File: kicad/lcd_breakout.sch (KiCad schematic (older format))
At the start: 3 parts

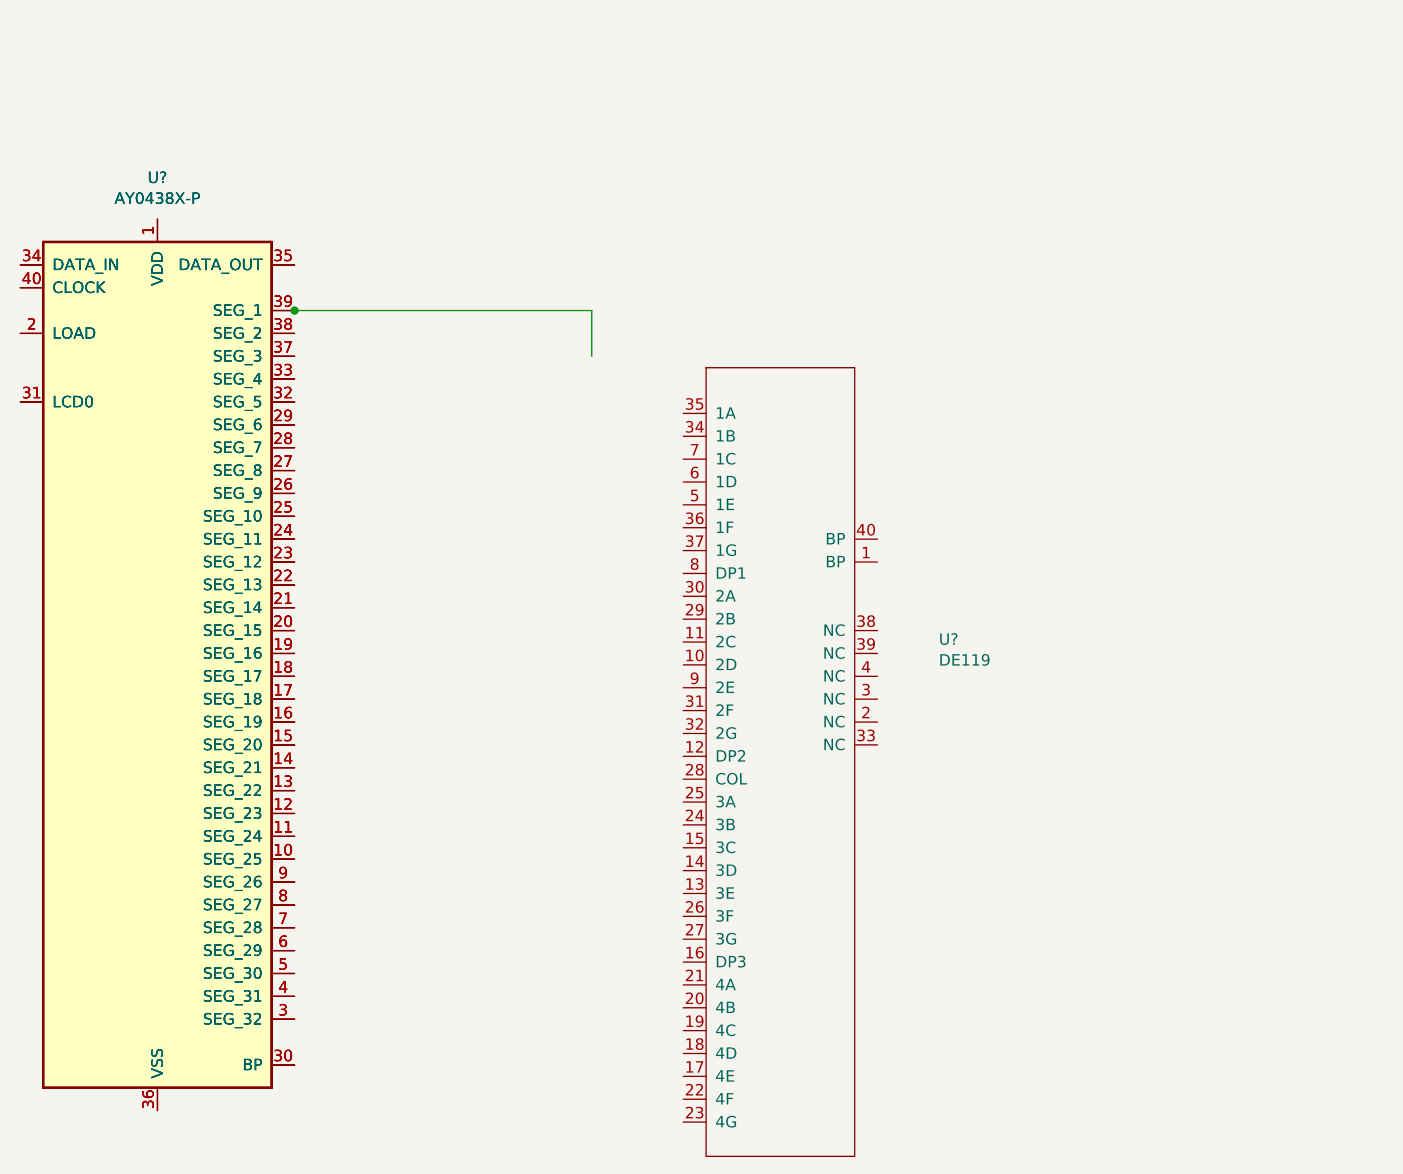
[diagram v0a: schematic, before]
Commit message: Update lcd component and schematic
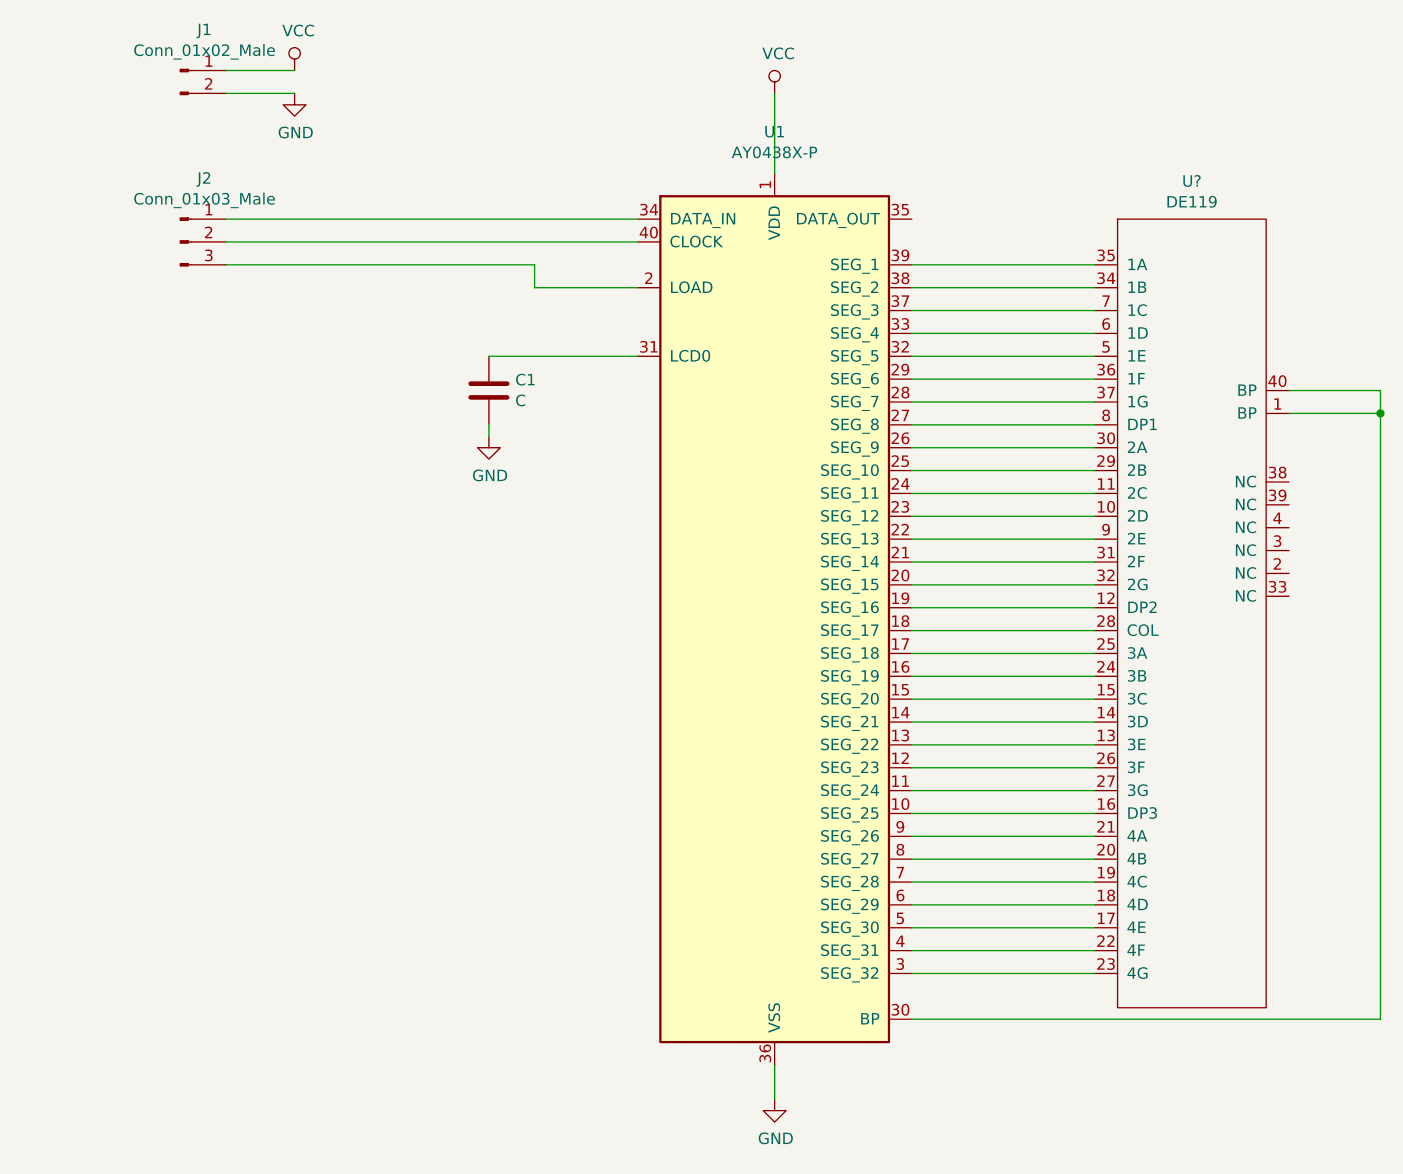
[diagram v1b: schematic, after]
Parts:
- removed U?: DE119, symbol lcd_breakout:DE119
- removed U?: AY0438X-P, Package_DIP:DIP-40_W15.24mm, symbol Driver_Display:AY0438X-P
- added C1: C, symbol Device:C
- added J1: Conn_01x02_Male, symbol Connector:Conn_01x02_Male
- added J2: Conn_01x03_Male, symbol Connector:Conn_01x03_Male
- added U?: DE119, symbol lcd_breakout:DE119
- gave numbers to parts that had none: 1
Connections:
- net labels added: GND, VCC
- wire segments 2 -> 48
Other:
- moved on the sheet: U1
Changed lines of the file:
@@
 EESchema Schematic File Version 4
-EELAYER 29 0
+LIBS:lcd_breakout-cache
+EELAYER 26 0
 EELAYER END
 $Descr A4 11693 8268
@@
 $EndDescr
 $Comp
+L Driver_Display:AY0438X-P U1
+U 1 1 5EA9573D
+P 4450 3550
+F 0 "U1" H 4450 5631 50  0000 C CNN
+F 1 "AY0438X-P" H 4450 5540 50  0000 C CNN
+F 2 "Package_DIP:DIP-40_W15.24mm" H 4450 1450 50  0001 C CNN
+F 3 "http://www.farnell.com/datasheets/43336.pdf" H 2850 4800 50  0001 C CNN
+	1    4450 3550
+	1    0    0    -1
+$EndComp
+$Comp
+L power:VCC #PWR0101
+U 1 1 5EA9E564
+P 4450 1300
+F 0 "#PWR0101" H 4450 1150 50  0001 C CNN
+F 1 "VCC" H 4467 1473 50  0000 C CNN
+F 2 "" H 4450 1300 50  0001 C CNN
+F 3 "" H 4450 1300 50  0001 C CNN
+	1    4450 1300
+	1    0    0    -1
+$EndComp
+$Comp
+L power:GND #PWR0102
+U 1 1 5EA9E718
+P 4450 5700
+F 0 "#PWR0102" H 4450 5450 50  0001 C CNN
+F 1 "GND" H 4455 5527 50  0000 C CNN
+F 2 "" H 4450 5700 50  0001 C CNN
+F 3 "" H 4450 5700 50  0001 C CNN
+	1    4450 5700
+	1    0    0    -1
+$EndComp
+Wire Wire Line
+	4450 5550 4450 5700
+Wire Wire Line
+	4450 1300 4450 1650
+$Comp
+L Connector:Conn_01x03_Male J2
+U 1 1 5EA9FA35
+P 1850 1950
+F 0 "J2" H 1956 2228 50  0000 C CNN
+F 1 "Conn_01x03_Male" H 1956 2137 50  0000 C CNN
+F 2 "" H 1850 1950 50  0001 C CNN
+F 3 "~" H 1850 1950 50  0001 C CNN
+	1    1850 1950
+	1    0    0    -1
+$EndComp
+$Comp
+L Connector:Conn_01x02_Male J1
+U 1 1 5EAA0729
+P 1850 1200
+F 0 "J1" H 1956 1378 50  0000 C CNN
+F 1 "Conn_01x02_Male" H 1956 1287 50  0000 C CNN
+F 2 "" H 1850 1200 50  0001 C CNN
+F 3 "~" H 1850 1200 50  0001 C CNN
+	1    1850 1200
+	1    0    0    -1
+$EndComp
+$Comp
+L power:GND #PWR0103
+U 1 1 5EAA09A4
+P 2350 1300
+F 0 "#PWR0103" H 2350 1050 50  0001 C CNN
+F 1 "GND" H 2355 1127 50  0000 C CNN
+F 2 "" H 2350 1300 50  0001 C CNN
+F 3 "" H 2350 1300 50  0001 C CNN
+	1    2350 1300
+	1    0    0    -1
+$EndComp
+$Comp
+L power:VCC #PWR0104
+U 1 1 5EAA0A11
+P 2350 1200
+F 0 "#PWR0104" H 2350 1050 50  0001 C CNN
+F 1 "VCC" H 2367 1373 50  0000 C CNN
+F 2 "" H 2350 1200 50  0001 C CNN
+F 3 "" H 2350 1200 50  0001 C CNN
+	1    2350 1200
+	1    0    0    -1
+$EndComp
+Wire Wire Line
+	2050 1200 2350 1200
+Wire Wire Line
+	2050 1300 2350 1300
+Wire Wire Line
+	2050 1850 3850 1850
+Wire Wire Line
+	2050 1950 3850 1950
+Wire Wire Line
+	2050 2050 3400 2050
+Wire Wire Line
+	3400 2050 3400 2150
+Wire Wire Line
+	3400 2150 3850 2150
+$Comp
+L Device:C C1
+U 1 1 5EAA22A5
+P 3200 2600
+F 0 "C1" H 3315 2646 50  0000 L CNN
+F 1 "C" H 3315 2555 50  0000 L CNN
+F 2 "" H 3238 2450 50  0001 C CNN
+F 3 "~" H 3200 2600 50  0001 C CNN
+	1    3200 2600
+	1    0    0    -1
+$EndComp
+Wire Wire Line
+	3200 2450 3850 2450
+$Comp
+L power:GND #PWR0105
+U 1 1 5EAA297E
+P 3200 2800
+F 0 "#PWR0105" H 3200 2550 50  0001 C CNN
+F 1 "GND" H 3205 2627 50  0000 C CNN
+F 2 "" H 3200 2800 50  0001 C CNN
+F 3 "" H 3200 2800 50  0001 C CNN
+	1    3200 2800
+	1    0    0    -1
+$EndComp
+Wire Wire Line
+	3200 2750 3200 2800
+$Comp
 L lcd_breakout:DE119 U?
-U 1 1 5EA94CD7
-P 4350 3900
-F 0 "U?" H 5168 4111 50  0000 L CNN
-F 1 "DE119" H 5168 4020 50  0000 L CNN
-F 2 "" H 4300 4300 50  0001 C CNN
-F 3 "" H 4300 4300 50  0001 C CNN
-	1    4350 3900
-	1    0    0    -1
-$EndComp
-$Comp
-L Driver_Display:AY0438X-P U?
-U 1 1 5EA9962D
-P 1750 3750
-F 0 "U?" H 1750 5831 50  0000 C CNN
-F 1 "AY0438X-P" H 1750 5740 50  0000 C CNN
-F 2 "Package_DIP:DIP-40_W15.24mm" H 1750 1650 50  0001 C CNN
-F 3 "http://www.farnell.com/datasheets/43336.pdf" H 150 5000 50  0001 C CNN
-	1    1750 3750
-	1    0    0    -1
-$EndComp
-$Comp
-L Driver_Display:AY0438X-P U?
-U 1 1 5EA9573D
-P 1750 3750
-F 0 "U?" H 1750 5831 50  0000 C CNN
-F 1 "AY0438X-P" H 1750 5740 50  0000 C CNN
-F 2 "Package_DIP:DIP-40_W15.24mm" H 1750 1650 50  0001 C CNN
-F 3 "http://www.farnell.com/datasheets/43336.pdf" H 150 5000 50  0001 C CNN
-	1    1750 3750
-	1    0    0    -1
-$EndComp
-Connection ~ 2350 2250
-Wire Wire Line
-	2350 2250 3650 2250
-Wire Wire Line
-	3650 2250 3650 2450
+U 1 1 5EAA427C
+P 6150 3250
+F 0 "U?" H 6275 4815 50  0000 C CNN
+F 1 "DE119" H 6275 4724 50  0000 C CNN
+F 2 "" H 7100 2450 50  0001 C CNN
+F 3 "" H 7100 2450 50  0001 C CNN
+	1    6150 3250
+	1    0    0    -1
+$EndComp
+Wire Wire Line
+	5050 2050 5850 2050
+Wire Wire Line
+	5050 2150 5850 2150
+Wire Wire Line
+	5050 2250 5850 2250
+Wire Wire Line
+	5050 2350 5850 2350
+Wire Wire Line
+	5050 2450 5850 2450
+Wire Wire Line
+	5050 2550 5850 2550
+Wire Wire Line
+	5050 2650 5850 2650
+Wire Wire Line
+	5050 2750 5850 2750
+Wire Wire Line
+	5050 2850 5850 2850
+Wire Wire Line
+	5050 2950 5850 2950
+Wire Wire Line
+	5050 3050 5850 3050
+Wire Wire Line
+	5050 3150 5850 3150
+Wire Wire Line
+	5050 3250 5850 3250
+Wire Wire Line
+	5050 3350 5850 3350
+Wire Wire Line
+	5050 3450 5850 3450
+Wire Wire Line
+	5050 3550 5850 3550
+Wire Wire Line
+	5050 3650 5850 3650
+Wire Wire Line
+	5050 3750 5850 3750
+Wire Wire Line
+	5050 3850 5850 3850
+Wire Wire Line
+	5050 3950 5850 3950
+Wire Wire Line
+	5050 4050 5850 4050
+Wire Wire Line
+	5050 4150 5850 4150
+Wire Wire Line
+	5050 4250 5850 4250
+Wire Wire Line
+	5050 4350 5850 4350
+Wire Wire Line
+	5050 4450 5850 4450
+Wire Wire Line
+	5050 4550 5850 4550
+Wire Wire Line
+	5050 4650 5850 4650
+Wire Wire Line
+	5050 4750 5850 4750
+Wire Wire Line
+	5050 4850 5850 4850
+Wire Wire Line
+	5050 4950 5850 4950
+Wire Wire Line
+	5050 5050 5850 5050
+Wire Wire Line
+	5050 5150 5850 5150
+Wire Wire Line
+	6700 2600 7100 2600
+Wire Wire Line
+	7100 5350 5050 5350
+Wire Wire Line
+	6700 2700 7100 2700
+Wire Wire Line
+	7100 2600 7100 2700
+Connection ~ 7100 2700
+Wire Wire Line
+	7100 2700 7100 5350
 $EndSCHEMATC

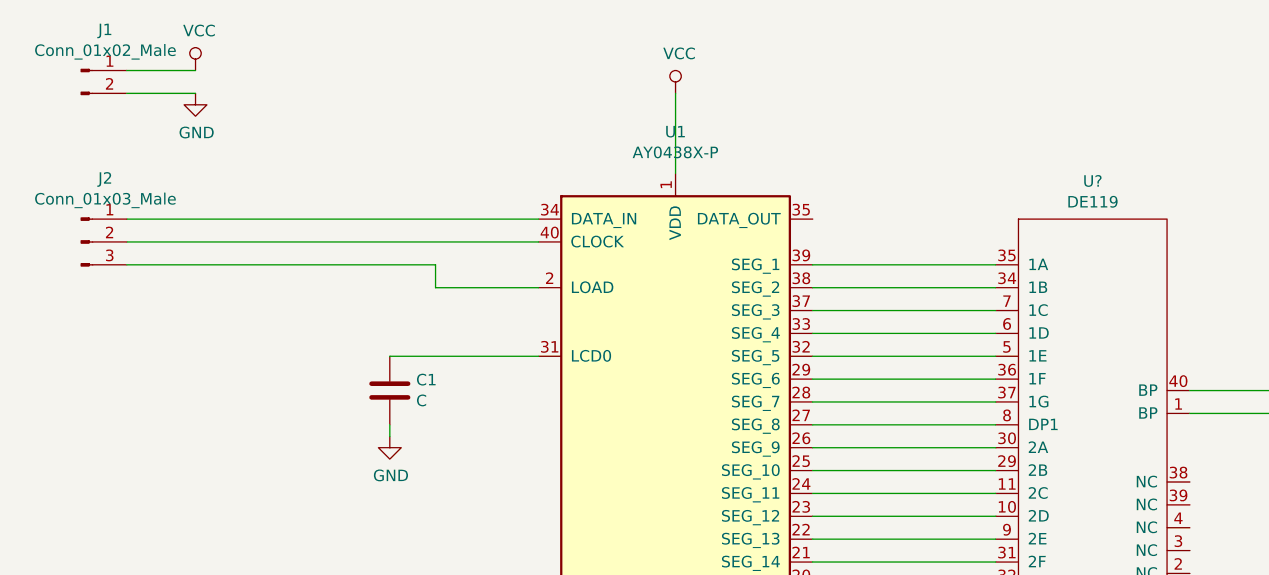
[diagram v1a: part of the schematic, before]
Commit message: Start placing board
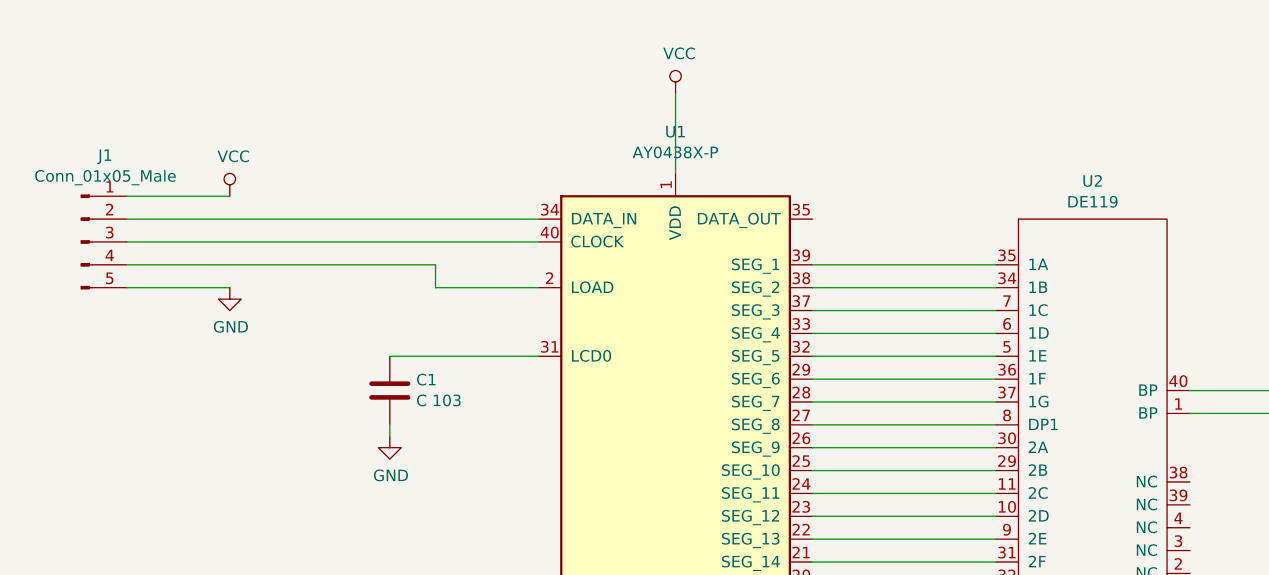
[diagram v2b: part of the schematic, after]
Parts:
- removed J1: Conn_01x02_Male, symbol Connector:Conn_01x02_Male
- removed J2: Conn_01x03_Male, symbol Connector:Conn_01x03_Male
- added J1: Conn_01x05_Male, Connector_PinHeader_2.54mm:PinHeader_1x05_P2.54mm_Vertical_SMD_Pin1Right, symbol Connector:Conn_01x05_Male
- C1: value C -> C 103; footprint (none) -> Capacitor_THT:C_Disc_D6.0mm_W4.4mm_P5.00mm
- U2: renamed from U?; footprint (none) -> kicad:DE119
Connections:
- net GND: now also J1.5 (Pin_5)
- net VCC: now also J1.1 (Pin_1)
- net at U1.2 (LOAD): now also J1.4 (Pin_4)
- net at U1.34 (DATA_IN): now also J1.2 (Pin_2)
- net at U1.40 (CLOCK): now also J1.3 (Pin_3)
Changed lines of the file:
@@
 $EndComp
 $Comp
-L power:VCC #PWR0101
+L power:VCC #PWR04
 U 1 1 5EA9E564
 P 4450 1300
-F 0 "#PWR0101" H 4450 1150 50  0001 C CNN
+F 0 "#PWR04" H 4450 1150 50  0001 C CNN
 F 1 "VCC" H 4467 1473 50  0000 C CNN
 F 2 "" H 4450 1300 50  0001 C CNN
@@
 $EndComp
 $Comp
-L power:GND #PWR0102
+L power:GND #PWR05
 U 1 1 5EA9E718
 P 4450 5700
-F 0 "#PWR0102" H 4450 5450 50  0001 C CNN
+F 0 "#PWR05" H 4450 5450 50  0001 C CNN
 F 1 "GND" H 4455 5527 50  0000 C CNN
 F 2 "" H 4450 5700 50  0001 C CNN
@@
 	4450 1300 4450 1650
 $Comp
-L Connector:Conn_01x03_Male J2
-U 1 1 5EA9FA35
-P 1850 1950
-F 0 "J2" H 1956 2228 50  0000 C CNN
-F 1 "Conn_01x03_Male" H 1956 2137 50  0000 C CNN
-F 2 "" H 1850 1950 50  0001 C CNN
-F 3 "~" H 1850 1950 50  0001 C CNN
-	1    1850 1950
+L power:GND #PWR02
+U 1 1 5EAA09A4
+P 2500 2150
+F 0 "#PWR02" H 2500 1900 50  0001 C CNN
+F 1 "GND" H 2505 1977 50  0000 C CNN
+F 2 "" H 2500 2150 50  0001 C CNN
+F 3 "" H 2500 2150 50  0001 C CNN
+	1    2500 2150
 	1    0    0    -1
 $EndComp
 $Comp
-L Connector:Conn_01x02_Male J1
-U 1 1 5EAA0729
-P 1850 1200
-F 0 "J1" H 1956 1378 50  0000 C CNN
-F 1 "Conn_01x02_Male" H 1956 1287 50  0000 C CNN
-F 2 "" H 1850 1200 50  0001 C CNN
-F 3 "~" H 1850 1200 50  0001 C CNN
-	1    1850 1200
+L power:VCC #PWR01
+U 1 1 5EAA0A11
+P 2500 1750
+F 0 "#PWR01" H 2500 1600 50  0001 C CNN
+F 1 "VCC" H 2517 1923 50  0000 C CNN
+F 2 "" H 2500 1750 50  0001 C CNN
+F 3 "" H 2500 1750 50  0001 C CNN
+	1    2500 1750
 	1    0    0    -1
 $EndComp
-$Comp
-L power:GND #PWR0103
-U 1 1 5EAA09A4
-P 2350 1300
-F 0 "#PWR0103" H 2350 1050 50  0001 C CNN
-F 1 "GND" H 2355 1127 50  0000 C CNN
-F 2 "" H 2350 1300 50  0001 C CNN
-F 3 "" H 2350 1300 50  0001 C CNN
-	1    2350 1300
-	1    0    0    -1
-$EndComp
-$Comp
-L power:VCC #PWR0104
-U 1 1 5EAA0A11
-P 2350 1200
-F 0 "#PWR0104" H 2350 1050 50  0001 C CNN
-F 1 "VCC" H 2367 1373 50  0000 C CNN
-F 2 "" H 2350 1200 50  0001 C CNN
-F 3 "" H 2350 1200 50  0001 C CNN
-	1    2350 1200
-	1    0    0    -1
-$EndComp
-Wire Wire Line
-	2050 1200 2350 1200
-Wire Wire Line
-	2050 1300 2350 1300
 Wire Wire Line
 	2050 1850 3850 1850
@@
 P 3200 2600
 F 0 "C1" H 3315 2646 50  0000 L CNN
-F 1 "C" H 3315 2555 50  0000 L CNN
-F 2 "" H 3238 2450 50  0001 C CNN
+F 1 "C 103" H 3315 2555 50  0000 L CNN
+F 2 "Capacitor_THT:C_Disc_D6.0mm_W4.4mm_P5.00mm" H 3238 2450 50  0001 C CNN
 F 3 "~" H 3200 2600 50  0001 C CNN
 	1    3200 2600
@@
 	3200 2450 3850 2450
 $Comp
-L power:GND #PWR0105
+L power:GND #PWR03
 U 1 1 5EAA297E
 P 3200 2800
-F 0 "#PWR0105" H 3200 2550 50  0001 C CNN
+F 0 "#PWR03" H 3200 2550 50  0001 C CNN
 F 1 "GND" H 3205 2627 50  0000 C CNN
 F 2 "" H 3200 2800 50  0001 C CNN
@@
 	3200 2750 3200 2800
 $Comp
-L lcd_breakout:DE119 U?
+L lcd_breakout:DE119 U2
 U 1 1 5EAA427C
 P 6150 3250
-F 0 "U?" H 6275 4815 50  0000 C CNN
+F 0 "U2" H 6275 4815 50  0000 C CNN
 F 1 "DE119" H 6275 4724 50  0000 C CNN
-F 2 "" H 7100 2450 50  0001 C CNN
+F 2 "kicad:DE119" H 7100 2450 50  0001 C CNN
 F 3 "" H 7100 2450 50  0001 C CNN
 	1    6150 3250
@@
 Wire Wire Line
 	7100 2700 7100 5350
+$Comp
+L Connector:Conn_01x05_Male J1
+U 1 1 5EABEDCF
+P 1850 1950
+F 0 "J1" H 1956 2328 50  0000 C CNN
+F 1 "Conn_01x05_Male" H 1956 2237 50  0000 C CNN
+F 2 "Connector_PinHeader_2.54mm:PinHeader_1x05_P2.54mm_Vertical_SMD_Pin1Right" H 1850 1950 50  0001 C CNN
+F 3 "~" H 1850 1950 50  0001 C CNN
+	1    1850 1950
+	1    0    0    -1
+$EndComp
+Wire Wire Line
+	2050 2150 2500 2150
+Wire Wire Line
+	2050 1750 2500 1750
 $EndSCHEMATC
